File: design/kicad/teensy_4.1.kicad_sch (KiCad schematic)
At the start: 3 parts, among them J10 Conn_01x24_Socket, J9 Conn_01x24_Socket

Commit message: Update kicad binary files
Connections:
- net 3V3: no longer J9.15 (Pin_15), MCU1.15 (3V3)
- no-connect marks 0 -> 2
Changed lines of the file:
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@@
 		(color 0 0 0 0)
 	)
-	(junction
+	(no_connect
+		(at 92.71 86.36)
+	)
+	(no_connect
 		(at 88.9 86.36)
-		(diameter 0)
-		(color 0 0 0 0)
 	)
 	(wire
@@
 	(wire
 		(pts
-			(xy 88.9 86.36) (xy 92.71 86.36)
-		)
-		(stroke
-			(width 0)
-			(type default)
-		)
-	)
-	(wire
-		(pts
 			(xy 88.9 83.82) (xy 92.71 83.82)
 		)
@@
 		(pts
 			(xy 161.29 50.8) (xy 152.4 50.8)
-		)
-		(stroke
-			(width 0)
-			(type default)
-		)
-	)
-	(wire
-		(pts
-			(xy 80.01 86.36) (xy 88.9 86.36)
 		)
 		(stroke
@@
 		(effects
 			(font
-				(size 1.27 1.27)
-			)
-			(justify right)
-		)
-	)
-	(hierarchical_label "3V3"
-		(shape input)
-		(at 80.01 86.36 180)
-		(effects
-			(font

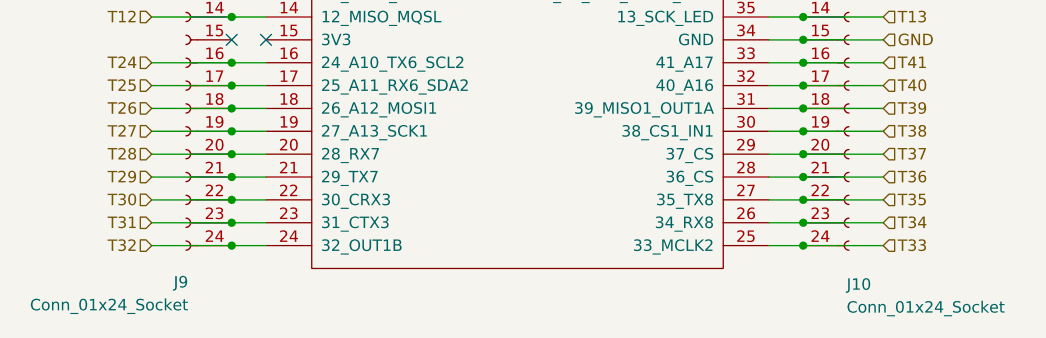
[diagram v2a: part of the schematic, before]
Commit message: Update kicad binary files
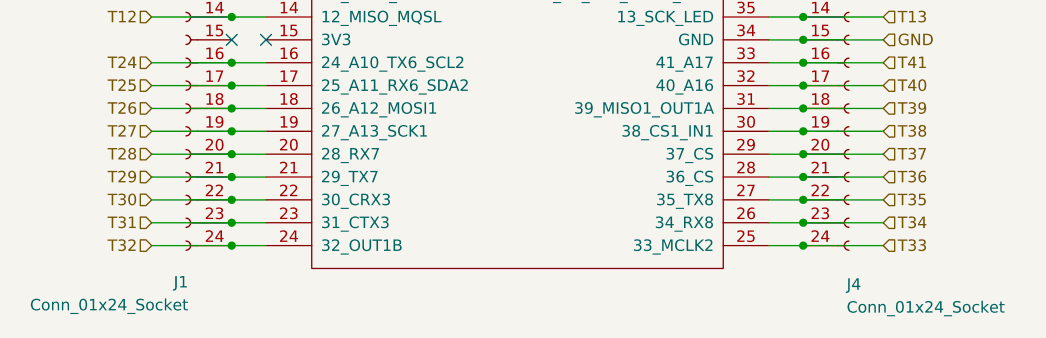
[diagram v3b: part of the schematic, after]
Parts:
- J1: renamed from J9; LCSC (none) -> C41376163
- J4: renamed from J10; LCSC (none) -> C41376163
- MCU1: now left out of the parts list
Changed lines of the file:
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@@
 		(on_board yes)
 		(dnp no)
-		(property "Reference" "J9"
+		(property "Reference" "J1"
 			(at 84.074 113.284 0)
 			(effects
@@
 		(property "Description" "Generic connector, single row, 01x24, script generated"
 			(at 83.82 78.74 0)
+			(effects
+				(font
+					(size 1.27 1.27)
+				)
+				(hide yes)
+			)
+		)
+		(property "LCSC" "C41376163"
+			(at 84.074 113.284 0)
 			(effects
 				(font
@@
 			(project "midi_controller"
 				(path "/9e44e663-00d0-4f33-bf1f-c4ad78deb554/40260c5c-6a74-49ce-9861-63e56838c401"
-					(reference "J9")
+					(reference "J1")
 					(unit 1)
 				)
@@
 		(on_board yes)
 		(dnp no)
-		(property "Reference" "J10"
+		(property "Reference" "J4"
 			(at 157.226 113.538 0)
 			(effects
@@
 		(property "Description" "Generic connector, single row, 01x24, script generated"
 			(at 157.48 78.74 0)
+			(effects
+				(font
+					(size 1.27 1.27)
+				)
+				(hide yes)
+			)
+		)
+		(property "LCSC" "C41376163"
+			(at 157.226 113.538 0)
 			(effects
 				(font
@@
 			(project "midi_controller"
 				(path "/9e44e663-00d0-4f33-bf1f-c4ad78deb554/40260c5c-6a74-49ce-9861-63e56838c401"
-					(reference "J10")
+					(reference "J4")
 					(unit 1)
 				)
@@
 		(unit 1)
 		(exclude_from_sim no)
-		(in_bom yes)
+		(in_bom no)
 		(on_board no)
 		(dnp no)

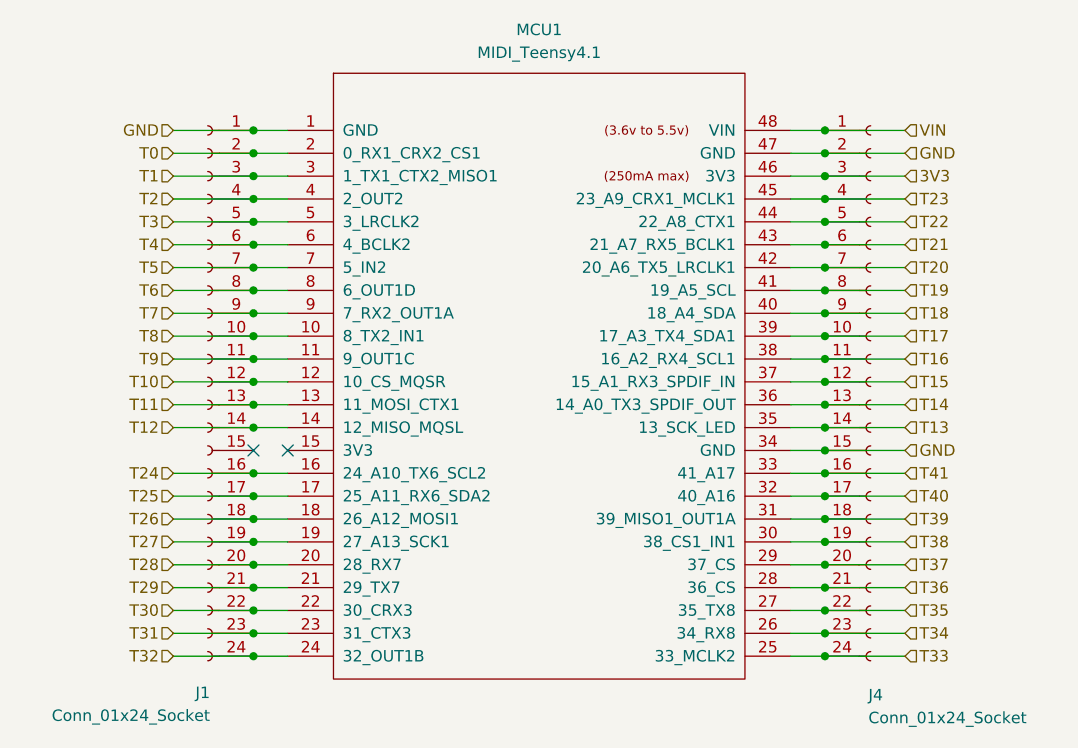
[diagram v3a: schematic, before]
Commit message: Update kicad binary files
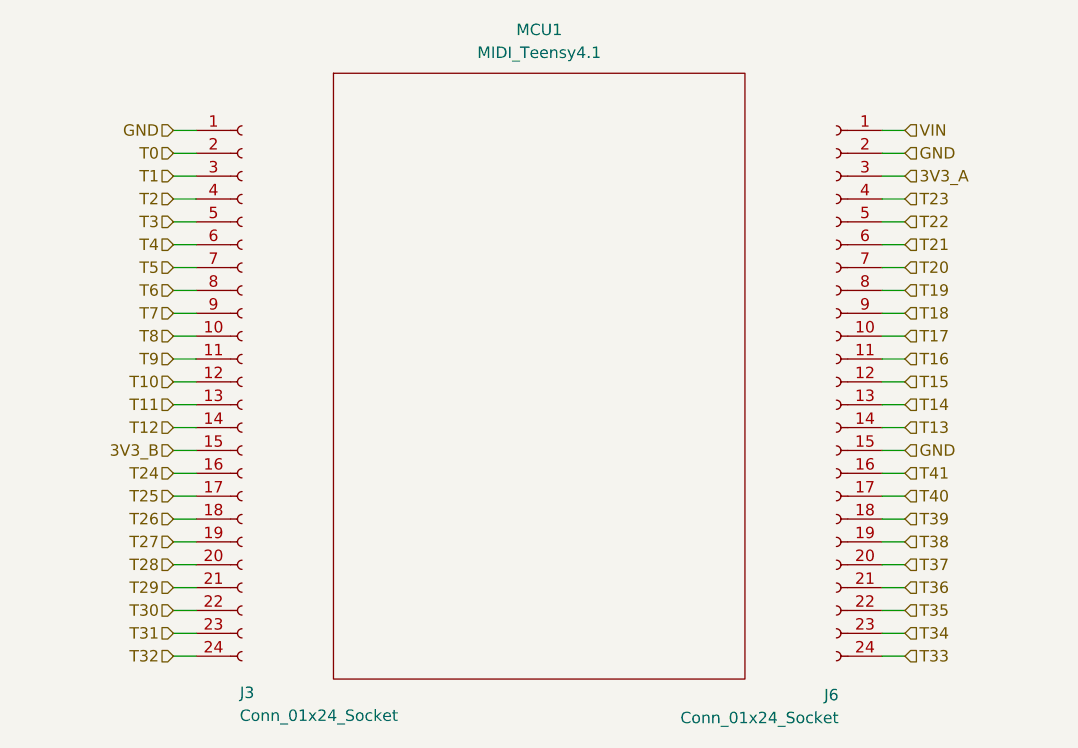
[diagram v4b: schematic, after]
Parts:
- J3: renamed from J1; footprint Connector_PinSocket_2.54mm:PinSocket_1x24_P2.54mm_Vertical -> midi_controller:PinSocket_1x24_P2.54mm_Vertical; symbol Connector:Conn_01x24_Socket -> midi_controller:Conn_01x24_Socket
- J6: renamed from J4; footprint Connector_PinSocket_2.54mm:PinSocket_1x24_P2.54mm_Vertical -> midi_controller:PinSocket_1x24_P2.54mm_Vertical; symbol Connector:Conn_01x24_Socket -> midi_controller:Conn_01x24_Socket
- MCU1: footprint midi_controller:Teensy41 -> midi_controller:Teensy41_Mechanical; symbol midi_controller:MIDI_Teensy4.1 -> midi_controller:MIDI_Teensy4.1_Graphical_only
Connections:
- net GND: no longer MCU1.1 (GND), MCU1.34 (GND), MCU1.47 (GND)
- net T0: no longer MCU1.2 (0_RX1_CRX2_CS1)
- net T1: no longer MCU1.3 (1_TX1_CTX2_MISO1)
- net T10: no longer MCU1.12 (10_CS_MQSR)
- net T11: no longer MCU1.13 (11_MOSI_CTX1)
- net T12: no longer MCU1.14 (12_MISO_MQSL)
- net T13: no longer MCU1.35 (13_SCK_LED)
- net T14: no longer MCU1.36 (14_A0_TX3_SPDIF_OUT)
- net T15: no longer MCU1.37 (15_A1_RX3_SPDIF_IN)
- net T16: no longer MCU1.38 (16_A2_RX4_SCL1)
- net T17: no longer MCU1.39 (17_A3_TX4_SDA1)
- net T18: no longer MCU1.40 (18_A4_SDA)
- net T19: no longer MCU1.41 (19_A5_SCL)
- net T2: no longer MCU1.4 (2_OUT2)
- net T20: no longer MCU1.42 (20_A6_TX5_LRCLK1)
- net T21: no longer MCU1.43 (21_A7_RX5_BCLK1)
- net T22: no longer MCU1.44 (22_A8_CTX1)
- net T23: no longer MCU1.45 (23_A9_CRX1_MCLK1)
- net T24: no longer MCU1.16 (24_A10_TX6_SCL2)
- net T25: no longer MCU1.17 (25_A11_RX6_SDA2)
- net T26: no longer MCU1.18 (26_A12_MOSI1)
- net T27: no longer MCU1.19 (27_A13_SCK1)
- net T28: no longer MCU1.20 (28_RX7)
- net T29: no longer MCU1.21 (29_TX7)
- net T3: no longer MCU1.5 (3_LRCLK2)
- net T30: no longer MCU1.22 (30_CRX3)
- net T31: no longer MCU1.23 (31_CTX3)
- net T32: no longer MCU1.24 (32_OUT1B)
- net T33: no longer MCU1.25 (33_MCLK2)
- net T34: no longer MCU1.26 (34_RX8)
- net T35: no longer MCU1.27 (35_TX8)
- net T36: no longer MCU1.28 (36_CS)
- net T37: no longer MCU1.29 (37_CS)
- net T38: no longer MCU1.30 (38_CS1_IN1)
- net T39: no longer MCU1.31 (39_MISO1_OUT1A)
- net T4: no longer MCU1.6 (4_BCLK2)
- net T40: no longer MCU1.32 (40_A16)
- net T41: no longer MCU1.33 (41_A17)
- net T5: no longer MCU1.7 (5_IN2)
- net T6: no longer MCU1.8 (6_OUT1D)
- net T7: no longer MCU1.9 (7_RX2_OUT1A)
- net T8: no longer MCU1.10 (8_TX2_IN1)
- net T9: no longer MCU1.11 (9_OUT1C)
- net VIN: no longer MCU1.48 (VIN)
- net 3V3_B: now reaches J3.15 (Pin_15)
- net 3V3 renamed 3V3_A
- net 3V3_A: no longer MCU1.46 (3V3)
- no-connect marks 2 -> 0
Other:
- moved on the sheet: J3, J6
